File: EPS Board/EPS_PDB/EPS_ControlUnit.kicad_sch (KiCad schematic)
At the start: 35 parts, among them Q1 PMOS, Q2 PMOS, SW1 SW_SPDT, U2 SN65HVD256D, U3 SN65HVD256D, U4 STM32L476VET6, U5 TPS3824-33QDBVRQ1, Y1 32MHz

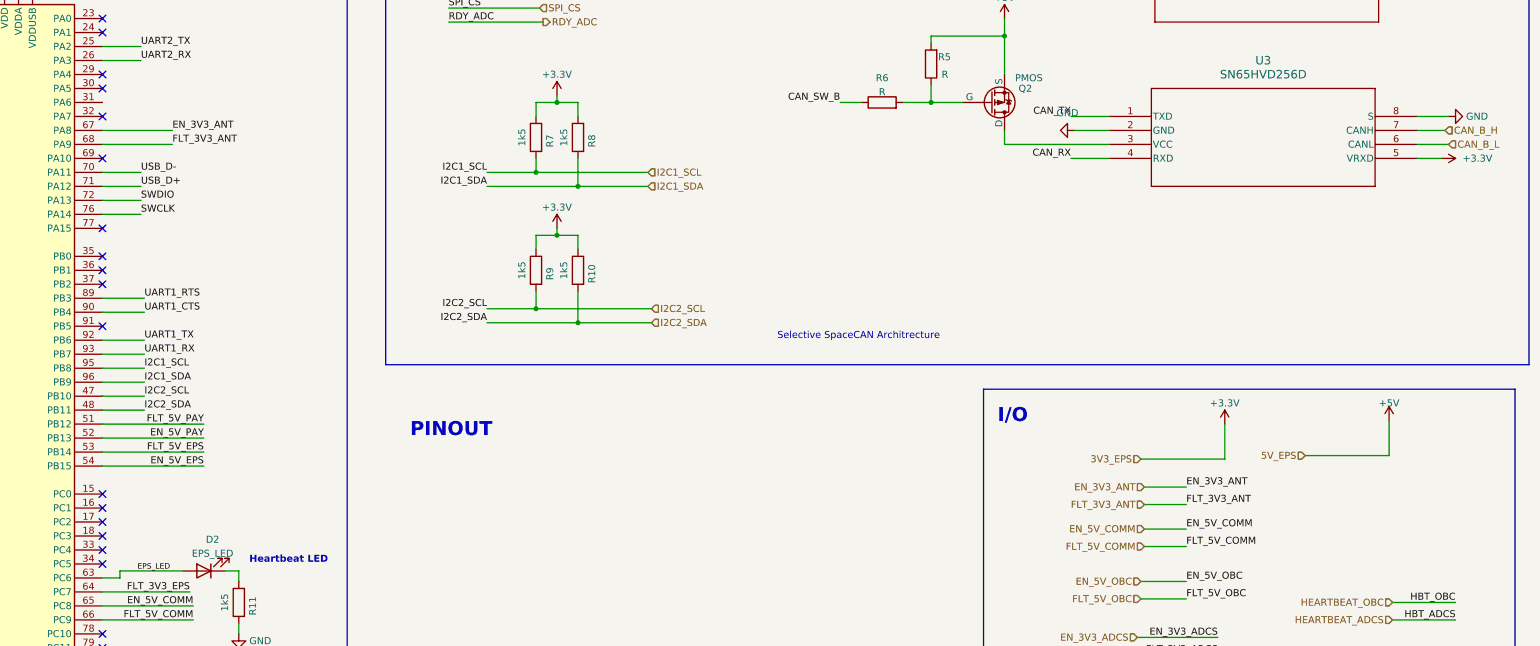
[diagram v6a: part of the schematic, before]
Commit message: PDB PCB Design Progress
Board outline copy pasted from Antenna Deployment Board
Added current limiter datasheet
Routed USB differential pair
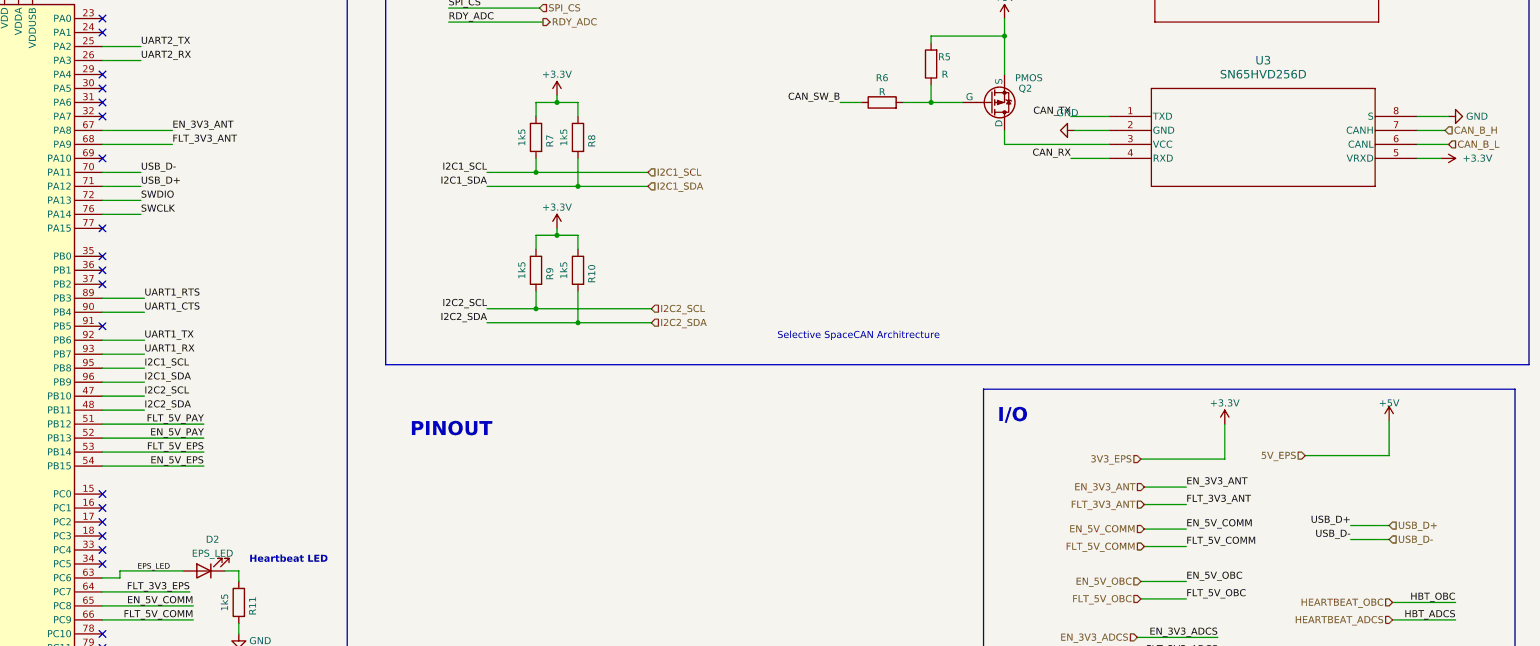
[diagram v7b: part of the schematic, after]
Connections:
- no-connect marks 33 -> 34
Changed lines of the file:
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@@
 		(at 95.25 123.825)
 	)
+	(no_connect
+		(at 140.97 98.425)
+	)
 	(wire
 		(pts
@@
 	(wire
 		(pts
+			(xy 374.65 177.8) (xy 367.665 177.8)
+		)
+		(stroke
+			(width 0)
+			(type default)
+		)
+	)
+	(wire
+		(pts
 			(xy 120.65 217.805) (xy 120.65 220.345)
 		)
@@
 		)
 	)
+	(wire
+		(pts
+			(xy 374.65 175.26) (xy 367.665 175.26)
+		)
+		(stroke
+			(width 0)
+			(type default)
+		)
+	)
 	(polyline
 		(pts
@@
 		)
 	)
+	(label "USB_D+"
+		(at 367.665 175.26 180)
+		(fields_autoplaced yes)
+		(effects
+			(font
+				(size 1.27 1.27)
+			)
+			(justify right bottom)
+		)
+	)
 	(label "SPI_CS"
 		(at 78.74 139.065 0)
@@
 		)
 	)
+	(label "USB_D-"
+		(at 367.665 177.8 180)
+		(fields_autoplaced yes)
+		(effects
+			(font
+				(size 1.27 1.27)
+			)
+			(justify right bottom)
+		)
+	)
 	(label "CAN_TX"
 		(at 316.865 100.965 180)
@@
 		)
 	)
+	(hierarchical_label "USB_D+"
+		(shape input)
+		(at 374.65 175.26 0)
+		(fields_autoplaced yes)
+		(effects
+			(font
+				(size 1.27 1.27)
+			)
+			(justify left)
+		)
+	)
 	(hierarchical_label "EN_5V_COMM"
 		(shape input)
@@
 		)
 	)
+	(hierarchical_label "USB_D-"
+		(shape input)
+		(at 374.65 177.8 0)
+		(fields_autoplaced yes)
+		(effects
+			(font
+				(size 1.27 1.27)
+			)
+			(justify left)
+		)
+	)

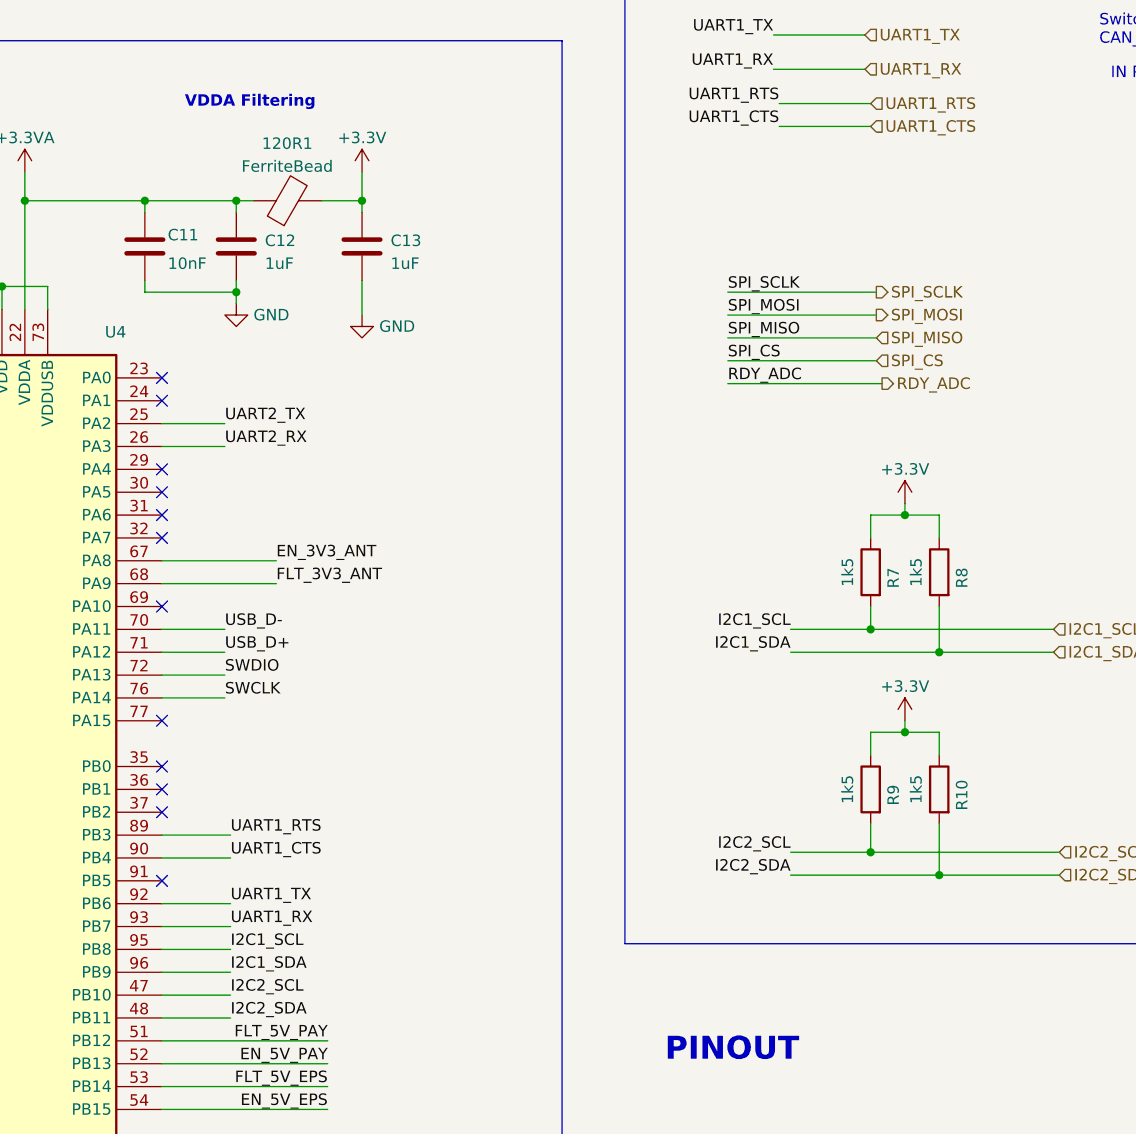
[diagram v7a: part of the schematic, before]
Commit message: EPS PDB Board Layout Progress
Fixed issue with outline,
added correct outline
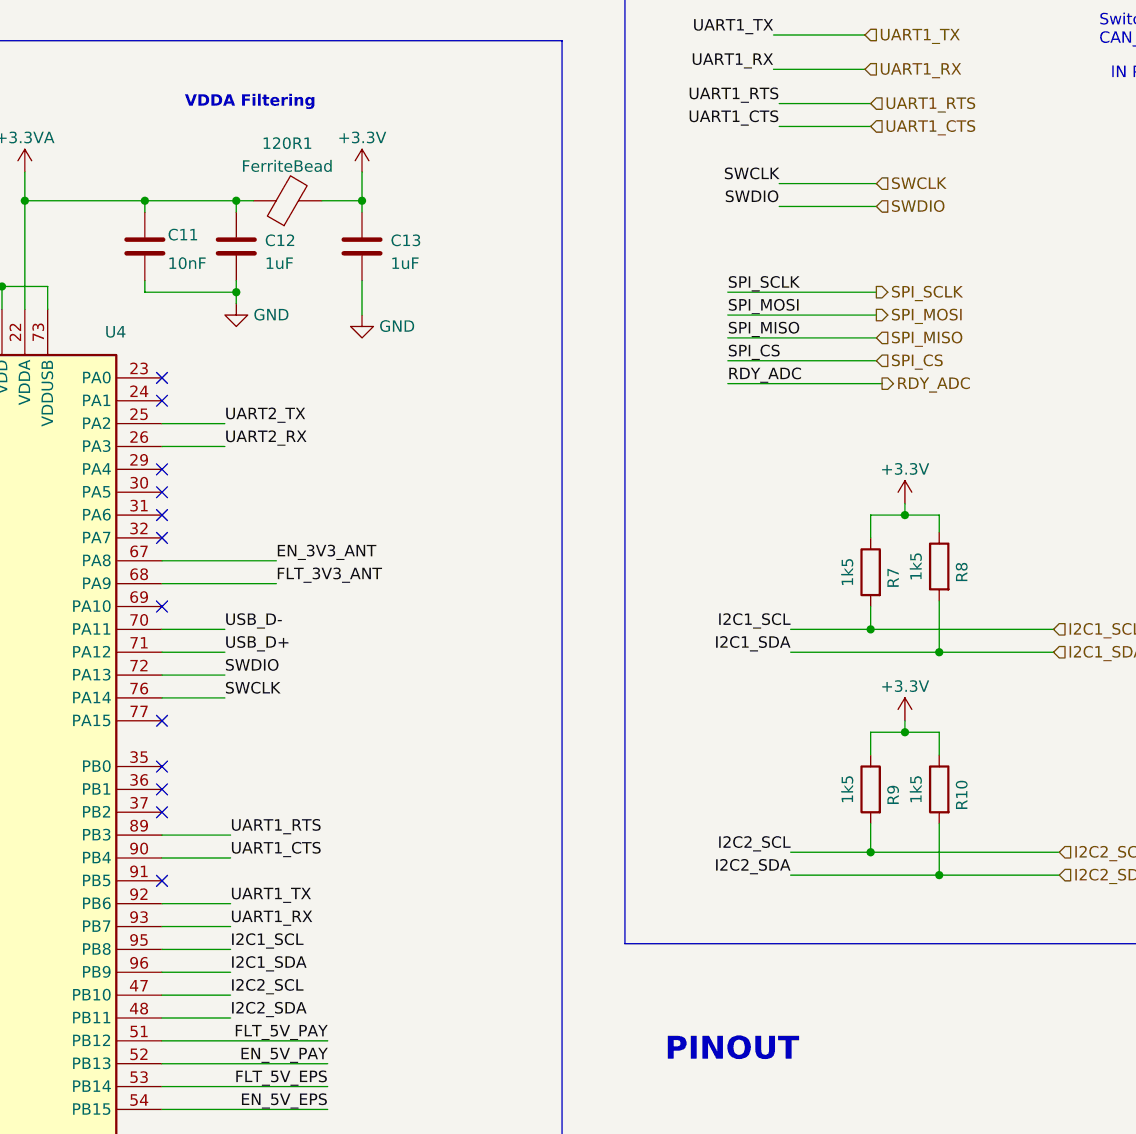
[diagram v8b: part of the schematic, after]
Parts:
- C10, C11, C12, C13, C14, C15, C16, C3, C4, C5, C6, C7, C8, C9: footprint Capacitor_SMD:C_0805_2012Metric -> Capacitor_SMD:C_0603_1608Metric
- R10, R11, R12, R2, R3, R4, R5, R6, R7, R8, R9: footprint Resistor_SMD:R_0805_2012Metric -> Resistor_SMD:R_0603_1608Metric
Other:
- moved on the sheet: R8
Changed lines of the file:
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@@
 	)
 	(junction
+		(at 227.33 113.665)
+		(diameter 0)
+		(color 0 0 0 0)
+	)
+	(junction
 		(at 50.8 60.325)
 		(diameter 0)
@@
 	)
 	(junction
-		(at 227.33 113.665)
-		(diameter 0)
-		(color 0 0 0 0)
-	)
-	(junction
 		(at 92.075 71.12)
 		(diameter 0)
@@
 	(wire
 		(pts
-			(xy 140.97 149.225) (xy 148.59 149.225)
-		)
-		(stroke
-			(width 0)
-			(type default)
-		)
-	)
-	(wire
-		(pts
 			(xy 47.625 107.95) (xy 47.625 123.19)
 		)
@@
 	(wire
 		(pts
-			(xy 227.33 98.425) (xy 227.33 100.965)
-		)
-		(stroke
-			(width 0)
-			(type default)
-		)
-	)
-	(wire
-		(pts
-			(xy 227.33 108.585) (xy 227.33 113.665)
+			(xy 227.33 98.425) (xy 227.33 100.33)
 		)
 		(stroke
@@
 	(wire
 		(pts
-			(xy 210.82 113.665) (xy 227.33 113.665)
-		)
-		(stroke
-			(width 0)
-			(type default)
-		)
-	)
-	(wire
-		(pts
 			(xy 128.27 73.025) (xy 123.19 73.025)
 		)
@@
 	(wire
 		(pts
+			(xy 227.33 113.665) (xy 240.03 113.665)
+		)
+		(stroke
+			(width 0)
+			(type default)
+		)
+	)
+	(wire
+		(pts
 			(xy 140.97 113.665) (xy 147.955 113.665)
 		)
@@
 	(wire
 		(pts
+			(xy 148.59 149.225) (xy 140.97 149.225)
+		)
+		(stroke
+			(width 0)
+			(type default)
+		)
+	)
+	(wire
+		(pts
 			(xy 227.33 122.555) (xy 227.33 125.095)
 		)
@@
 	(wire
 		(pts
+			(xy 220.345 64.135) (xy 209.55 64.135)
+		)
+		(stroke
+			(width 0)
+			(type default)
+		)
+	)
+	(wire
+		(pts
 			(xy 31.115 259.715) (xy 28.575 259.715)
 		)
@@
 	(wire
 		(pts
+			(xy 220.345 61.595) (xy 209.55 61.595)
+		)
+		(stroke
+			(width 0)
+			(type default)
+		)
+	)
+	(wire
+		(pts
 			(xy 330.2 171.45) (xy 337.82 171.45)
 		)
@@
 	(wire
 		(pts
-			(xy 227.33 113.665) (xy 240.03 113.665)
+			(xy 210.82 113.665) (xy 227.33 113.665)
 		)
 		(stroke
@@
 	(wire
 		(pts
+			(xy 227.33 107.95) (xy 227.33 113.665)
+		)
+		(stroke
+			(width 0)
+			(type default)
+		)
+	)
+	(wire
+		(pts
 			(xy 50.165 85.725) (xy 54.61 85.725)
 		)
@@
 		)
 	)
-	(label "I2C1_SDA"
-		(at 210.82 113.665 180)
-		(fields_autoplaced yes)
-		(effects
-			(font
-				(size 1.27 1.27)
-			)
-			(justify right bottom)
-		)
-	)
 	(label "CAN_SW_B"
 		(at 84.455 159.385 0)
@@
 		)
 	)
+	(label "I2C1_SDA"
+		(at 210.82 113.665 180)
+		(fields_autoplaced yes)
+		(effects
+			(font
+				(size 1.27 1.27)
+			)
+			(justify right bottom)
+		)
+	)
 	(label "STATUS_5V"
 		(at 80.01 128.905 0)
@@
 		)
 	)
+	(label "SWDIO"
+		(at 209.55 64.135 180)
+		(fields_autoplaced yes)
+		(effects
+			(font
+				(size 1.27 1.27)
+			)
+			(justify right bottom)
+		)
+	)
 	(label "EN_3V3_ADCS"
 		(at 79.375 179.705 0)
@@
 		)
 	)
+	(label "I2C1_SDA"
+		(at 148.59 149.225 0)
+		(fields_autoplaced yes)
+		(effects
+			(font
+				(size 1.27 1.27)
+			)
+			(justify left bottom)
+		)
+	)
 	(label "HBT_ADCS"
 		(at 81.915 116.205 0)
@@
 		)
 	)
+	(label "SWCLK"
+		(at 209.55 61.595 180)
+		(fields_autoplaced yes)
+		(effects
+			(font
+				(size 1.27 1.27)
+			)
+			(justify right bottom)
+		)
+	)
 	(label "ANT_DEPLOY"
 		(at 380.365 229.235 180)
@@
 		)
 	)
-	(label "I2C1_SDA"
-		(at 148.59 149.225 0)
-		(fields_autoplaced yes)
-		(effects
-			(font
-				(size 1.27 1.27)
-			)
-			(justify left bottom)
-		)
-	)
 	(label "I2C2_SCL"
 		(at 210.82 135.89 180)
@@
 		)
 	)
+	(hierarchical_label "SWDIO"
+		(shape input)
+		(at 220.345 64.135 0)
+		(fields_autoplaced yes)
+		(effects
+			(font
+				(size 1.27 1.27)
+			)
+			(justify left)
+		)
+	)
 	(hierarchical_label "RESET_ADC"
 		(shape output)
@@
 		)
 	)
+	(hierarchical_label "SWCLK"
+		(shape input)
+		(at 220.345 61.595 0)
+		(fields_autoplaced yes)
+		(effects
+			(font
+				(size 1.27 1.27)
+			)
+			(justify left)
+		)
+	)
 	(hierarchical_label "SPI_MISO"
 		(shape input)
@@
 			)
 		)
-		(property "Footprint" "Capacitor_SMD:C_0805_2012Metric"
+		(property "Footprint" "Capacitor_SMD:C_0603_1608Metric"
 			(at 93.0402 69.85 0)
 			(effects
@@
 	(symbol
 		(lib_id "Device:R")
-		(at 227.33 104.775 0)
+		(at 227.33 104.14 0)
 		(mirror y)
 		(unit 1)
@@
 		(dnp no)
 		(property "Reference" "R8"
-			(at 229.87 105.41 90)
+			(at 229.87 104.775 90)
 			(effects
 				(font
@@
 		)
 		(property "Value" "1k5"
-			(at 224.79 104.775 90)
+			(at 224.79 104.14 90)
 			(effects
 				(font
@@
 			)
 		)
-		(property "Footprint" "Resistor_SMD:R_0805_2012Metric"
-			(at 229.108 104.775 90)
+		(property "Footprint" "Resistor_SMD:R_0603_1608Metric"
+			(at 229.108 104.14 90)
 			(effects
 				(font
@@
 		)
 		(property "Datasheet" "~"
-			(at 227.33 104.775 0)
+			(at 227.33 104.14 0)
 			(effects
 				(font
@@
 		)
 		(property "Description" ""
-			(at 227.33 104.775 0)
+			(at 227.33 104.14 0)
 			(effects
 				(font
@@
 			)
 		)
-		(property "Footprint" "Capacitor_SMD:C_0805_2012Metric"
+		(property "Footprint" "Capacitor_SMD:C_0603_1608Metric"
 			(at 64.4652 132.715 0)
 			(effects
@@
 			)
 		)
-		(property "Footprint" "Resistor_SMD:R_0805_2012Metric"
+		(property "Footprint" "Resistor_SMD:R_0603_1608Metric"
 			(at 229.108 128.905 90)
 			(effects
@@
 			)
 		)
-		(property "Footprint" "Capacitor_SMD:C_0805_2012Metric"
+		(property "Footprint" "Capacitor_SMD:C_0603_1608Metric"
 			(at 42.2402 69.85 0)
 			(effects
@@
 			)
 		)
-		(property "Footprint" "Resistor_SMD:R_0805_2012Metric"
+		(property "Footprint" "Resistor_SMD:R_0603_1608Metric"
 			(at 282.575 100.203 90)
 			(effects
@@
 			)
 		)
-		(property "Footprint" "Capacitor_SMD:C_0805_2012Metric"
+		(property "Footprint" "Capacitor_SMD:C_0603_1608Metric"
 			(at 70.8152 69.85 0)
 			(effects
@@
 			)
 		)
-		(property "Footprint" "Resistor_SMD:R_0805_2012Metric"
+		(property "Footprint" "Resistor_SMD:R_0603_1608Metric"
 			(at 78.74 86.487 90)
 			(effects
@@
 			)
 		)
-		(property "Footprint" "Capacitor_SMD:C_0805_2012Metric"
+		(property "Footprint" "Capacitor_SMD:C_0603_1608Metric"
 			(at 61.2902 69.85 0)
 			(effects
@@
 			)
 		)
-		(property "Footprint" "Resistor_SMD:R_0805_2012Metric"
+		(property "Footprint" "Resistor_SMD:R_0603_1608Metric"
 			(at 113.665 264.033 90)
 			(effects
@@
 			)
 		)
-		(property "Footprint" "Capacitor_SMD:C_0805_2012Metric"
+		(property "Footprint" "Capacitor_SMD:C_0603_1608Metric"
 			(at 140.0302 72.39 0)
 			(effects
@@
 			)
 		)
-		(property "Footprint" "Capacitor_SMD:C_0805_2012Metric"
+		(property "Footprint" "Capacitor_SMD:C_0603_1608Metric"
 			(at 150.1902 72.39 0)
 			(effects
@@
 			)
 		)
-		(property "Footprint" "Capacitor_SMD:C_0805_2012Metric"
+		(property "Footprint" "Capacitor_SMD:C_0603_1608Metric"
 			(at 32.7152 69.85 0)
 			(effects
@@
 			)
 		)
-		(property "Footprint" "Resistor_SMD:R_0805_2012Metric"
+		(property "Footprint" "Resistor_SMD:R_0603_1608Metric"
 			(at 293.243 91.44 90)
 			(effects
@@
 			)
 		)
-		(property "Footprint" "Resistor_SMD:R_0805_2012Metric"
+		(property "Footprint" "Resistor_SMD:R_0603_1608Metric"
 			(at 221.488 128.905 90)
 			(effects
@@
 			)
 		)
-		(property "Footprint" "Resistor_SMD:R_0805_2012Metric"
+		(property "Footprint" "Resistor_SMD:R_0603_1608Metric"
 			(at 221.488 104.775 90)
 			(effects
@@
 			)
 		)
-		(property "Footprint" "Resistor_SMD:R_0805_2012Metric"
+		(property "Footprint" "Resistor_SMD:R_0603_1608Metric"
 			(at 282.575 70.358 90)
 			(effects
@@
 			)
 		)
-		(property "Footprint" "Resistor_SMD:R_0805_2012Metric"
+		(property "Footprint" "Resistor_SMD:R_0603_1608Metric"
 			(at 167.513 189.23 90)
 			(effects
@@
 			)
 		)
-		(property "Footprint" "Capacitor_SMD:C_0805_2012Metric"
+		(property "Footprint" "Capacitor_SMD:C_0603_1608Metric"
 			(at 42.2402 131.445 0)
 			(effects
@@
 			)
 		)
-		(property "Footprint" "Capacitor_SMD:C_0805_2012Metric"
+		(property "Footprint" "Capacitor_SMD:C_0603_1608Metric"
 			(at 164.1602 72.39 0)
 			(effects
@@
 			)
 		)
-		(property "Footprint" "Capacitor_SMD:C_0805_2012Metric"
+		(property "Footprint" "Capacitor_SMD:C_0603_1608Metric"
 			(at 39.0652 93.345 0)
 			(effects
@@
 			)
 		)
-		(property "Footprint" "Capacitor_SMD:C_0805_2012Metric"
+		(property "Footprint" "Capacitor_SMD:C_0603_1608Metric"
 			(at 103.2002 69.85 0)
 			(effects
@@
 			)
 		)
-		(property "Footprint" "Capacitor_SMD:C_0805_2012Metric"
+		(property "Footprint" "Capacitor_SMD:C_0603_1608Metric"
 			(at 51.7652 69.85 0)
 			(effects
@@
 			)
 		)
-		(property "Footprint" "Resistor_SMD:R_0805_2012Metric"
+		(property "Footprint" "Resistor_SMD:R_0603_1608Metric"
 			(at 293.878 62.865 90)
 			(effects
@@
 			)
 		)
-		(property "Footprint" "Capacitor_SMD:C_0805_2012Metric"
+		(property "Footprint" "Capacitor_SMD:C_0603_1608Metric"
 			(at 81.6102 69.85 0)
 			(effects
